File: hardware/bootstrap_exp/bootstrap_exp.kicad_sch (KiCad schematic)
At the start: 19 parts

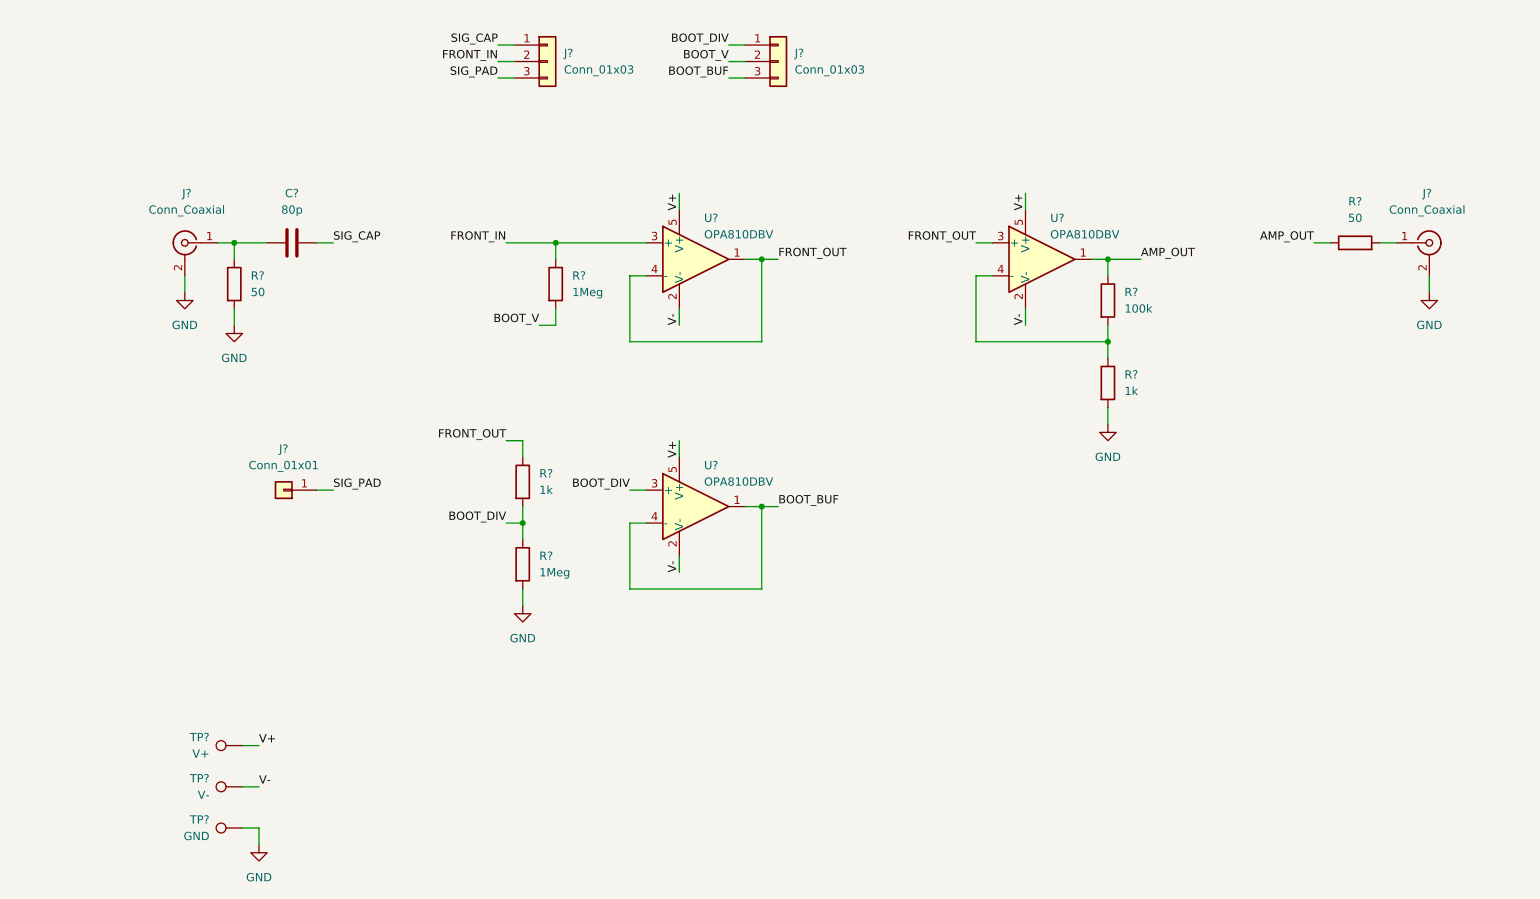
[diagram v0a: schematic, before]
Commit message: Add decoupling and test points
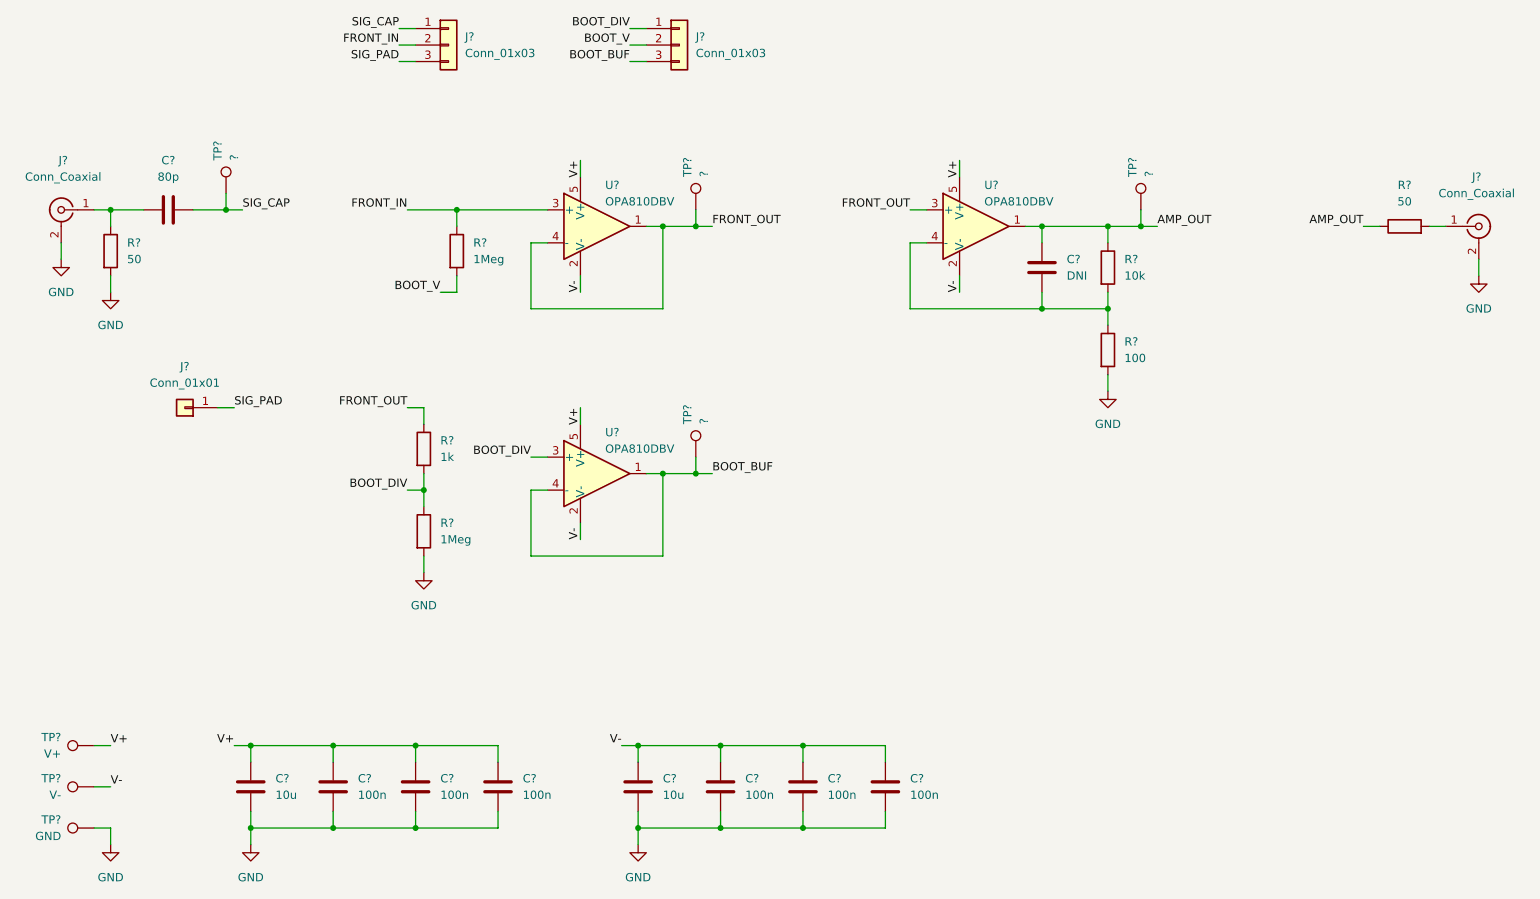
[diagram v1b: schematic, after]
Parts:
- added C? (x2): 10u, symbol Device:C
- added C? (x6): 100n, symbol Device:C
- added C?: DNI, symbol Device:C
- added TP? (x4): ?, symbol Connector:TestPoint
- R?: value 1k -> 100
- R?: value 100k -> 10k
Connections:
- net AMP_OUT: now also C?.1, TP?.1
- net BOOT_BUF: now also TP?.1
- net FRONT_OUT: now also TP?.1
- net GND: now also C?.2, C?.2, C?.2, C?.2, C?.2, C?.2, C?.2, C?.2
- net SIG_CAP: now also TP?.1
- net V+: now also C?.1, C?.1, C?.1, C?.1
- net V-: now also C?.1, C?.1, C?.1, C?.1
- net at R?.1, R?.2, U?.4 (-): now also C?.2
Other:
- moved on the sheet: C?, J?, R?, TP?, U?

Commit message: Assign initial footprints for layout checks
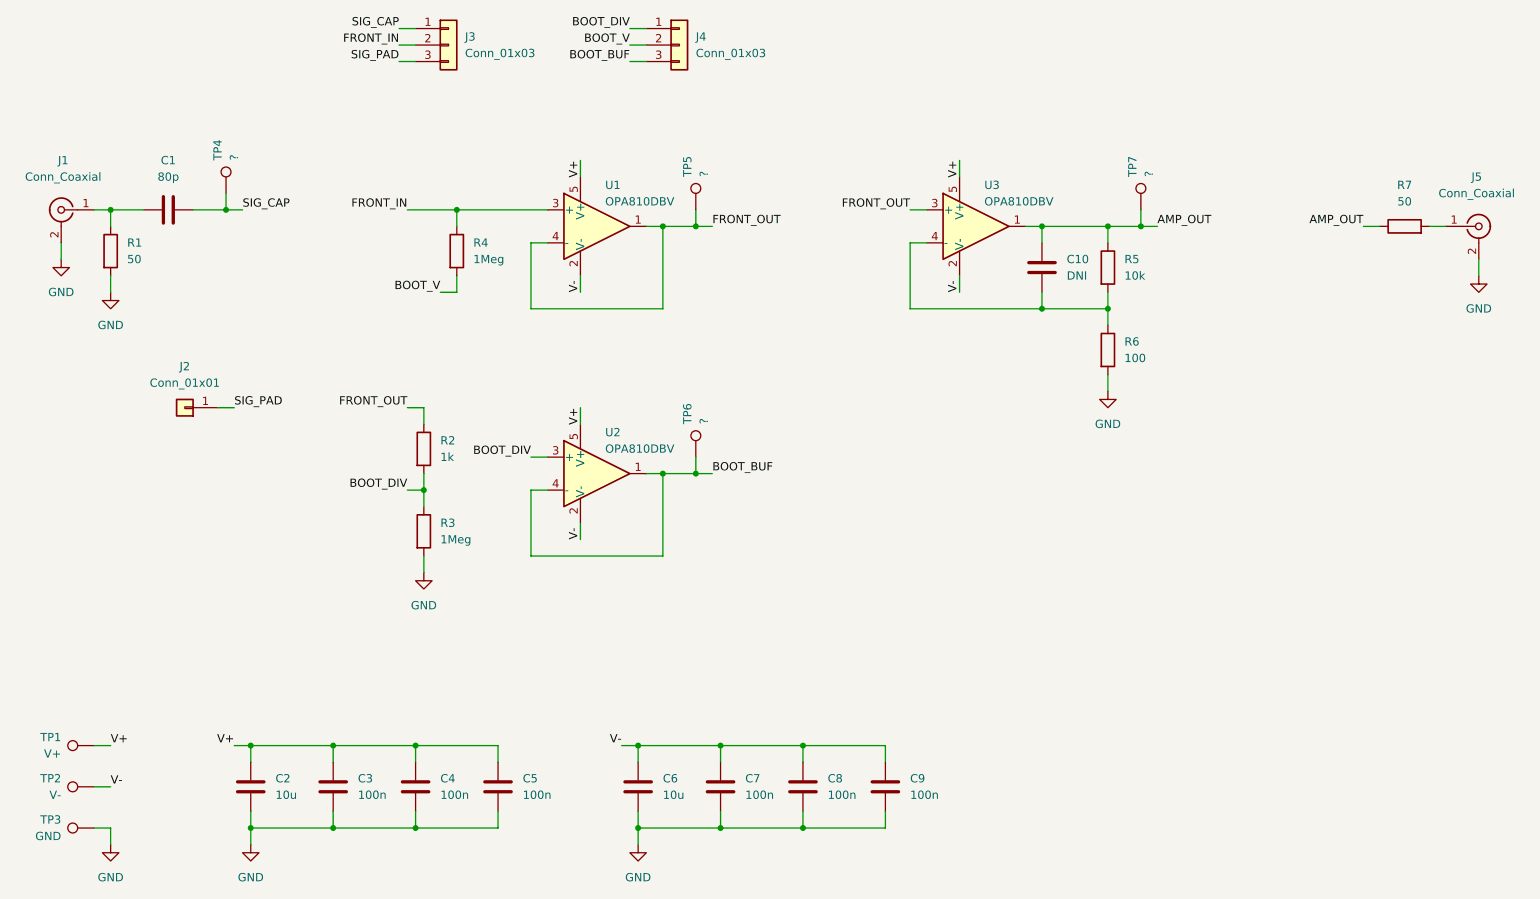
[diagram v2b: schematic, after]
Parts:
- C1, C10, C2, C3, C4, C5, C6, C7, C8, C9: renamed from C?; footprint (none) -> Capacitor_SMD:C_0603_1608Metric
- J1, J5: renamed from J?; footprint (none) -> Connector_Coaxial:SMA_Samtec_SMA-J-P-X-ST-EM1_EdgeMount
- J2: renamed from J?; footprint (none) -> local_footprints:Patch_Electrode_25x25mm
- J3, J4: renamed from J?; footprint (none) -> Connector_PinHeader_2.54mm:PinHeader_1x03_P2.54mm_Vertical
- R1, R2, R3, R4, R5, R6, R7: renamed from R?; footprint (none) -> Resistor_SMD:R_0603_1608Metric
- TP1, TP2, TP3, TP4, TP5, TP6, TP7: renamed from TP?; footprint (none) -> TestPoint:TestPoint_Keystone_5005-5009_Compact
- gave numbers to parts that had none: 3

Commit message: Remove sensitive pad and replace headers with jumper resistors
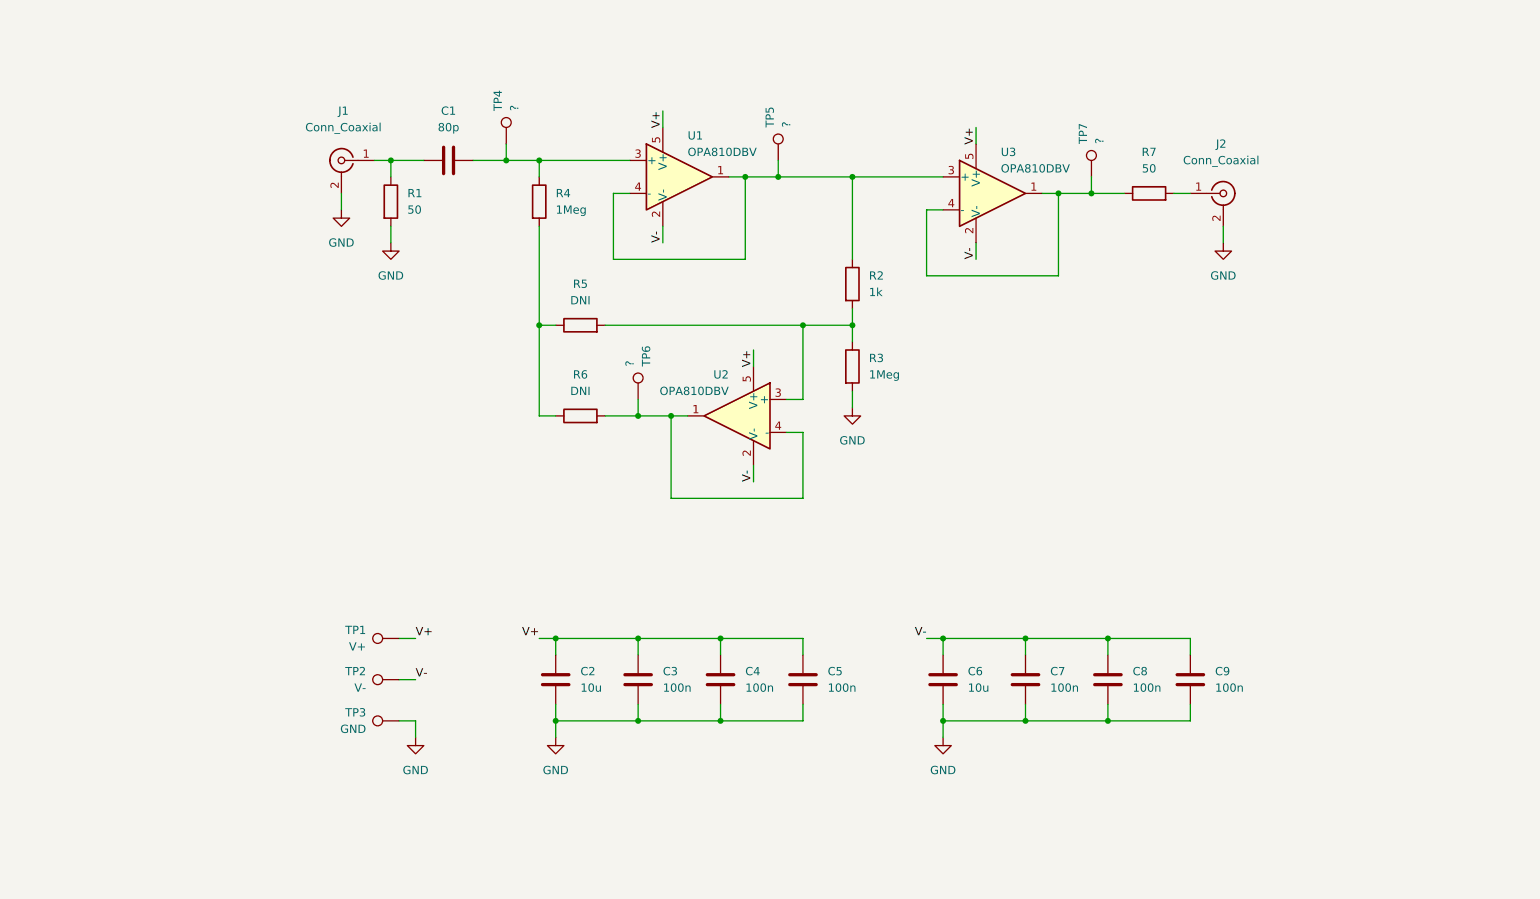
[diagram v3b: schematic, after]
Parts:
- removed C10: DNI, Capacitor_SMD:C_0603_1608Metric, symbol Device:C
- removed J2: Conn_01x01, local_footprints:Patch_Electrode_25x25mm, symbol Connector_Generic:Conn_01x01
- removed J3, J4: Conn_01x03, Connector_PinHeader_2.54mm:PinHeader_1x03_P2.54mm_Vertical, symbol Connector_Generic:Conn_01x03
- R5: value 10k -> DNI; footprint Resistor_SMD:R_0603_1608Metric -> (none)
- R6: value 100 -> DNI; footprint Resistor_SMD:R_0603_1608Metric -> (none)
- renumbered J5 to J2
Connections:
- net SIG_CAP is gone; now on an unnamed net: C1.1, TP4.1
- net GND: no longer R6.2
- net AMP_OUT: no longer names the net of R7.1, TP7.1, U3.1
- net AMP_OUT: now also U3.4 (-); no longer R5.1
- net BOOT_BUF: no longer names the net of TP6.1, U2.1, U2.4 (-)
- net BOOT_BUF: now also R6.2
- net BOOT_DIV: no longer names the net of R2.2, R3.1, U2.3 (+)
- net BOOT_DIV: now also R5.2
- net BOOT_V: no longer names the net of R4.2
- net BOOT_V: now also R5.1, R6.1
- net FRONT_IN: no longer names the net of R4.1, U1.3 (+)
- net FRONT_OUT: no longer names the net of R2.1, TP5.1, U1.1, U1.4 (-), U3.3 (+)
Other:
- moved on the sheet: C1, C2, C3, C4, C5, C6, C7, C8, C9, J1, J2, R1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

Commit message: Assign missing footprints
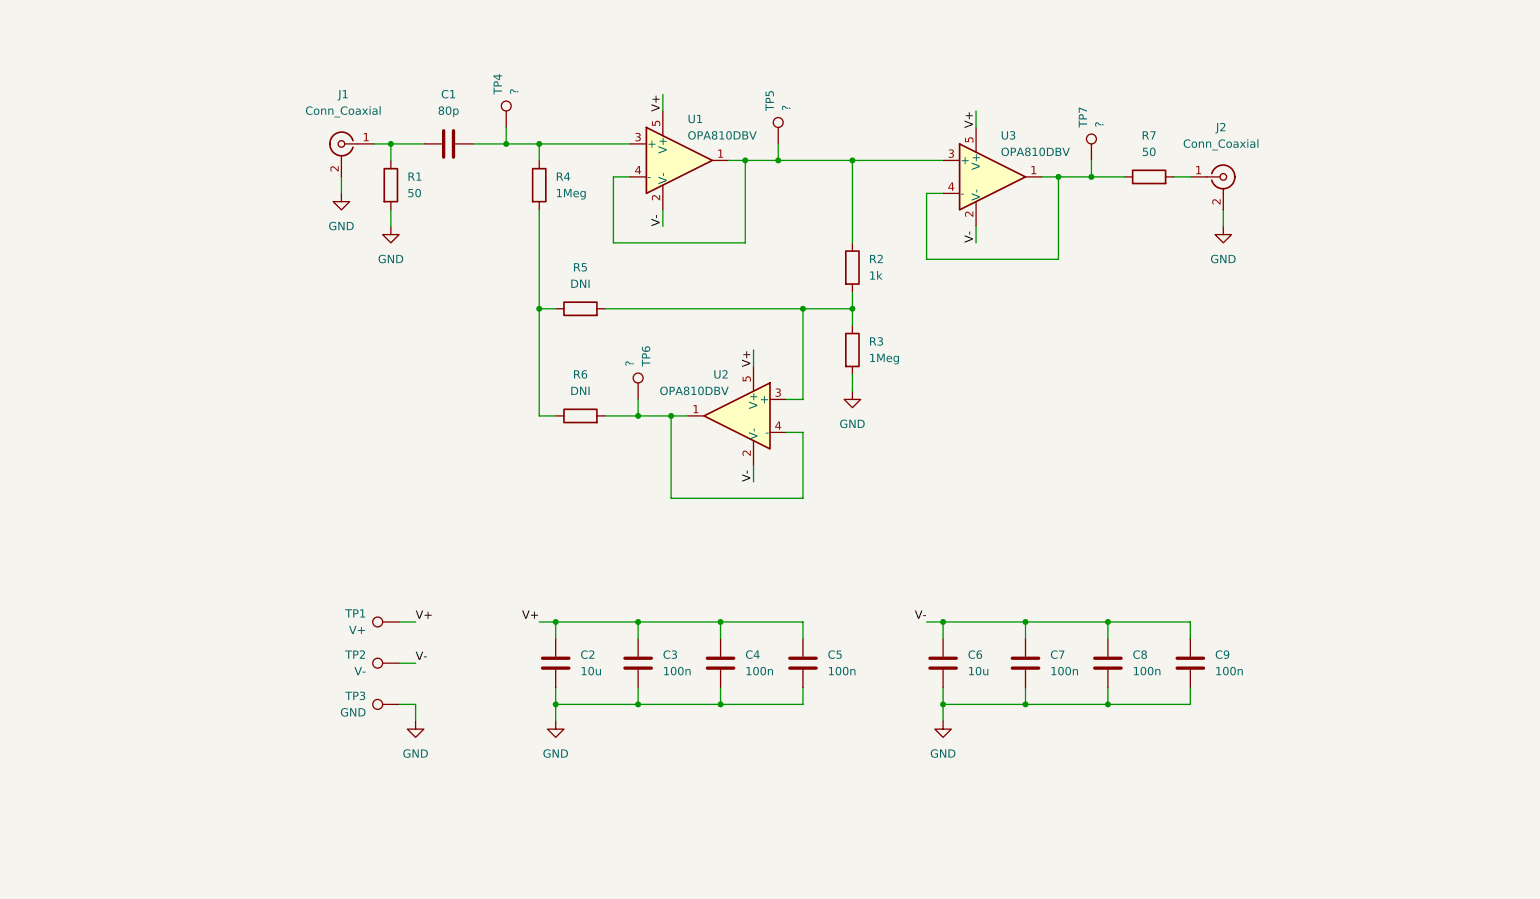
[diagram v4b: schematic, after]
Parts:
- R5, R6: footprint (none) -> Resistor_SMD:R_0603_1608Metric
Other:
- moved on the sheet: C1, C2, C3, C4, C5, C6, C7, C8, C9, J1, J2, R1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

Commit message: Remove test point for bootstrapped high-Z node
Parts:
- removed TP4: ?, TestPoint:TestPoint_Keystone_5005-5009_Compact, symbol Connector:TestPoint
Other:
- moved on the sheet: C1
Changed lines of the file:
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@@
   (junction (at 195.58 132.08) (diameter 0) (color 0 0 0 0)
   )
-  (junction (at 102.87 58.42) (diameter 0) (color 0 0 0 0)
-  )
   (junction (at 187.96 63.5) (diameter 0) (color 0 0 0 0)
   )
@@
     (stroke (width 0) (type default) (color 0 0 0 0))
   )
-  (wire (pts (xy 85.09 58.42) (xy 90.17 58.42))
+  (wire (pts (xy 85.09 58.42) (xy 92.71 58.42))
     (stroke (width 0) (type default) (color 0 0 0 0))
   )
@@
     (stroke (width 0) (type default) (color 0 0 0 0))
   )
-  (wire (pts (xy 97.79 58.42) (xy 102.87 58.42))
-    (stroke (width 0) (type default) (color 0 0 0 0))
-  )
   (wire (pts (xy 148.59 97.79) (xy 146.05 97.79))
     (stroke (width 0) (type default) (color 0 0 0 0))
@@
     (stroke (width 0) (type default) (color 0 0 0 0))
   )
-  (wire (pts (xy 102.87 55.88) (xy 102.87 58.42))
-    (stroke (width 0) (type default) (color 0 0 0 0))
-  )
   (wire (pts (xy 167.64 132.08) (xy 170.18 132.08))
     (stroke (width 0) (type default) (color 0 0 0 0))
@@
     (stroke (width 0) (type default) (color 0 0 0 0))
   )
-  (wire (pts (xy 102.87 58.42) (xy 107.95 58.42))
+  (wire (pts (xy 100.33 58.42) (xy 107.95 58.42))
     (stroke (width 0) (type default) (color 0 0 0 0))
   )
@@
     (pin "2")
   )
-  (symbol (lib_id "Connector:TestPoint") (at 102.87 55.88 0) (unit 1)
-    (in_bom yes) (on_board yes)
-    (property "Reference" "TP4" (id 0) (at 101.6 50.8 90)
-      (effects (font (size 1.27 1.27)) (justify left))
-    )
-    (property "Value" "?" (id 1) (at 104.14 50.8 90)
-      (effects (font (size 1.27 1.27)) (justify left))
-    )
-    (property "Footprint" "TestPoint:TestPoint_Keystone_5005-5009_Compact" (id 2) (at 107.95 55.88 0)
-      (effects (font (size 1.27 1.27)) hide)
-    )
-    (property "Datasheet" "~" (id 3) (at 107.95 55.88 0)
-      (effects (font (size 1.27 1.27)) hide)
-    )
-    (pin "1")
-  )
   (symbol (lib_id "Device:R") (at 114.3 83.82 90) (unit 1)
     (in_bom yes) (on_board yes) (fields_autoplaced)
@@
     (pin "1")
   )
-  (symbol (lib_id "Device:C") (at 93.98 58.42 270) (unit 1)
-    (in_bom yes) (on_board yes) (fields_autoplaced)
-    (property "Reference" "C1" (id 0) (at 93.98 50.8 90))
-    (property "Value" "80p" (id 1) (at 93.98 53.34 90))
-    (property "Footprint" "Capacitor_SMD:C_0603_1608Metric" (id 2) (at 90.17 59.3852 0)
-      (effects (font (size 1.27 1.27)) hide)
-    )
-    (property "Datasheet" "~" (id 3) (at 93.98 58.42 0)
+  (symbol (lib_id "Device:C") (at 96.52 58.42 270) (unit 1)
+    (in_bom yes) (on_board yes) (fields_autoplaced)
+    (property "Reference" "C1" (id 0) (at 96.52 50.8 90))
+    (property "Value" "80p" (id 1) (at 96.52 53.34 90))
+    (property "Footprint" "Capacitor_SMD:C_0603_1608Metric" (id 2) (at 92.71 59.3852 0)
+      (effects (font (size 1.27 1.27)) hide)
+    )
+    (property "Datasheet" "~" (id 3) (at 96.52 58.42 0)
       (effects (font (size 1.27 1.27)) hide)
     )
@@
       (reference "TP3") (unit 1) (value "GND") (footprint "TestPoint:TestPoint_Keystone_5005-5009_Compact")
     )
-    (path "/241a9dce-8fa3-4c13-899d-8fdcd0c723f7"
-      (reference "TP4") (unit 1) (value "?") (footprint "TestPoint:TestPoint_Keystone_5005-5009_Compact")
-    )
     (path "/11c63355-1c86-496d-b8dc-ecec6581d03f"
